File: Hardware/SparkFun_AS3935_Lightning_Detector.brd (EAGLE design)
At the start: 25.4 x 25.4 mm, 59 parts, among them U1 AS3935

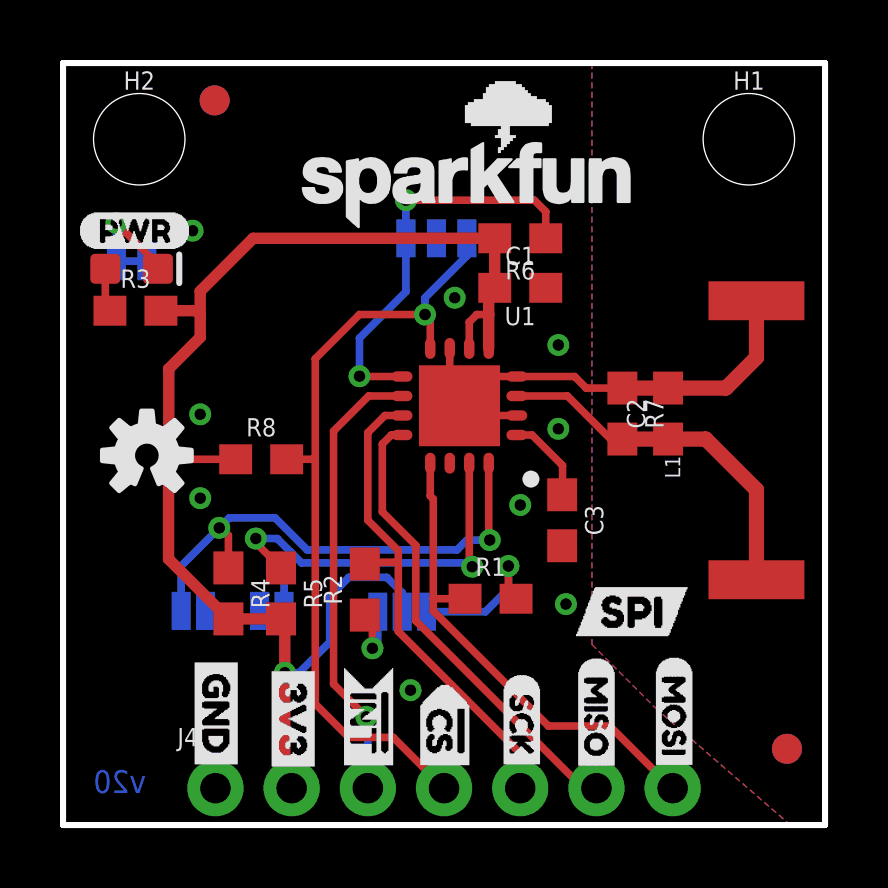
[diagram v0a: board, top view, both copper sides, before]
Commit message: Fixes interrupt label
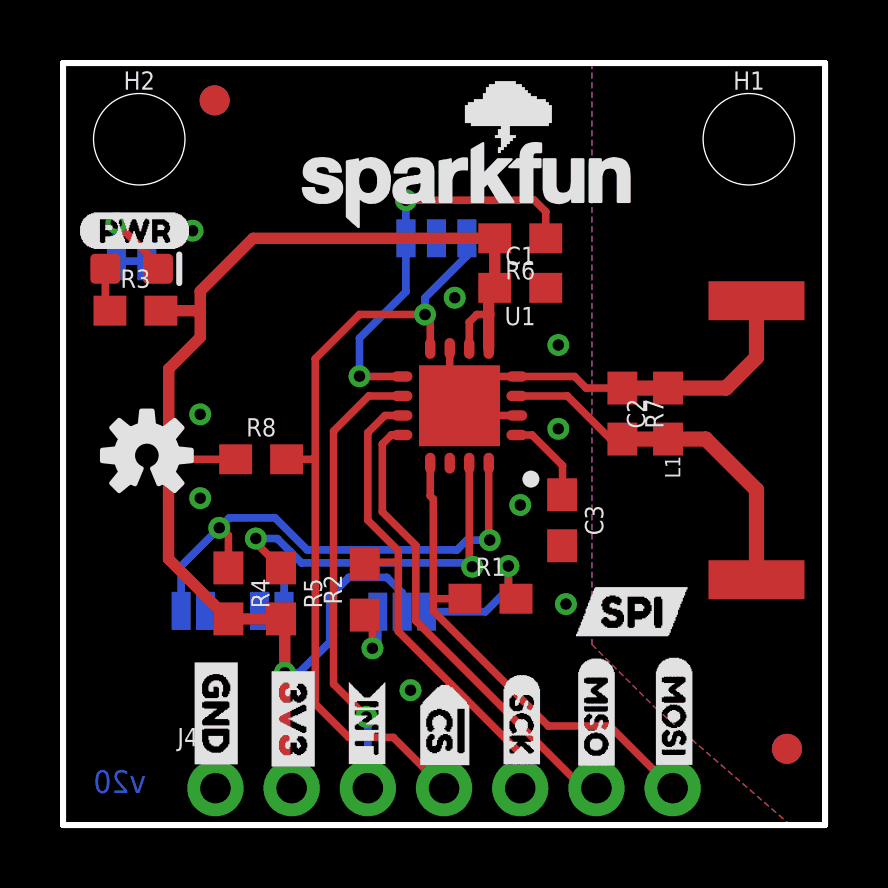
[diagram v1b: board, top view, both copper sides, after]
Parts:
- U$13, U$14: device INT:#INT0 -> buzzard_labels:INT0
- moved U$13 0.66 mm to (10.1, 4.85)
- moved U$14 0.66 mm to (10.1, 4.85)
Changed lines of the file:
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@@
 <layer number="45" name="Holes" color="7" fill="1" visible="yes" active="yes"/>
 <layer number="46" name="Milling" color="3" fill="1" visible="no" active="yes"/>
-<layer number="47" name="Measures" color="7" fill="1" visible="yes" active="yes"/>
+<layer number="47" name="Measures" color="7" fill="1" visible="no" active="yes"/>
 <layer number="48" name="Document" color="7" fill="1" visible="no" active="yes"/>
 <layer number="49" name="Reference" color="13" fill="1" visible="yes" active="yes"/>
@@
 <layer number="115" name="ReferenceISLANDS" color="7" fill="1" visible="no" active="no"/>
 <layer number="116" name="Patch_BOT" color="9" fill="4" visible="no" active="no"/>
-<layer number="117" name="PM_Ref" color="26" fill="1" visible="no" active="yes"/>
+<layer number="117" name="PM_Ref" color="26" fill="1" visible="yes" active="yes"/>
 <layer number="118" name="Rect_Pads" color="7" fill="1" visible="no" active="no"/>
-<layer number="119" name="PF_Ref" color="31" fill="1" visible="no" active="yes"/>
-<layer number="120" name="WFL_Ref" color="25" fill="1" visible="no" active="yes"/>
+<layer number="119" name="PF_Ref" color="31" fill="1" visible="yes" active="yes"/>
+<layer number="120" name="WFL_Ref" color="25" fill="1" visible="yes" active="yes"/>
 <layer number="121" name="_tsilk" color="7" fill="1" visible="no" active="no"/>
 <layer number="122" name="_bsilk" color="7" fill="1" visible="no" active="no"/>
@@
 <element name="U$9" library="Labels" package="MISO-(]-03" value="" x="17.78" y="5.6388" smashed="yes" rot="MR270"/>
 <element name="U$11" library="Labels" package="MOSI-(]-03" value="" x="20.3708" y="5.6642" smashed="yes" rot="MR270"/>
-<element name="U$13" library="INT" package="#INT0" value="" x="10.1854" y="5.5118" smashed="yes" rot="R270"/>
-<element name="U$14" library="INT" package="#INT0" value="" x="10.1854" y="5.5118" smashed="yes" rot="MR270"/>
 <element name="U$15" library="DataLines" package="SPI1" value="" x="21.082" y="7.112" smashed="yes" rot="MR0"/>
 <element name="U$17" library="i2c_EN" package="I#C_EN0" value="" x="15.367" y="21.6916" smashed="yes" rot="MR0"/>
@@
 <element name="U$16" library="CS and SI" package="CS0" value="" x="17.2212" y="19.5072" smashed="yes" rot="MR0"/>
 <element name="U$19" library="CS and SI" package="SI1" value="" x="11.176" y="19.4818" smashed="yes" rot="MR0"/>
+<element name="U$13" library="buzzard_labels" package="INT0" value="" x="10.1346" y="4.8514" smashed="yes" rot="R270"/>
+<element name="U$14" library="buzzard_labels" package="INT0" value="" x="10.1346" y="4.8514" smashed="yes" rot="MR270"/>
 </elements>
 <signals>
